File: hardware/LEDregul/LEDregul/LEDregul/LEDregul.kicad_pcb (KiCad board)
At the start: 2 copper layers, 62.7 x 57.1 mm, 45 parts, among them J1 Conn_02x04_Odd_Even, J2 Conn_01x04_Male, J4 Conn_01x20_Female, U1 FAN5341, U2 FAN5341, U3 FAN5341, U4 FAN5341, X1 SiT1534

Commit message: nRF52 start
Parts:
- moved R1 115.3 mm to (142.2, 95.2)
- moved R2 115.3 mm to (139.2, 95.2)
- moved R3 115.3 mm to (145.1, 95.2)
- moved R4 115.3 mm to (148.0, 95.2)
- moved U3 80.0 mm to (175.1, 68.6)
- moved C2 80.0 mm to (179.1, 61.8)
- moved C5 80.0 mm to (170.9, 72.0)
- moved C7 80.0 mm to (179.1, 65.1)
- moved D17 80.0 mm to (170.9, 68.7)
- moved D10 80.0 mm to (173.5, 61.9)
- moved D18 80.0 mm to (173.5, 65.3)
- moved C6 74.6 mm to (165.2, 78.8)
- moved D11 74.6 mm to (167.9, 65.3)
- moved D14 74.6 mm to (165.3, 75.5)
- moved D16 74.6 mm to (165.3, 72.1)
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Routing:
- net GND: track 198.2 -> 0.00 mm, vias 55 -> 0
- net +3V3: track 177.7 -> 0.00 mm, vias 3 -> 0
- net Net-(C1-Pad1): track 87.5 -> 0.00 mm
- net C1: track 64.9 -> 0.00 mm, vias 1 -> 0
- net Net-(D5-Pad1): track 64.4 -> 0.00 mm, vias 2 -> 0
- net Net-(C3-Pad1): track 63.3 -> 0.00 mm
- net C3: track 62.9 -> 0.00 mm, vias 1 -> 0
- net Net-(J4-Pad17): track 62.2 -> 0.00 mm
- net Net-(D15-Pad1): track 62.1 -> 0.00 mm, vias 2 -> 0
- net Net-(L2-Pad2): track 57.1 -> 0.00 mm, vias 2 -> 0
- net Net-(C7-Pad1): track 53.9 -> 0.00 mm
- net Net-(D20-Pad1): track 53.5 -> 0.00 mm
- net C2: track 51.6 -> 0.00 mm, vias 1 -> 0
- net Net-(D10-Pad1): track 46.6 -> 0.00 mm, vias 2 -> 0
- net Net-(BT1-Pad1): track 42.9 -> 0.00 mm
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- removed copper zone on B.Cu, net GND
- removed copper zone on F.Cu, net GND
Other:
- board size 62.7 x 57.1 mm -> 97.8 x 67.3 mm

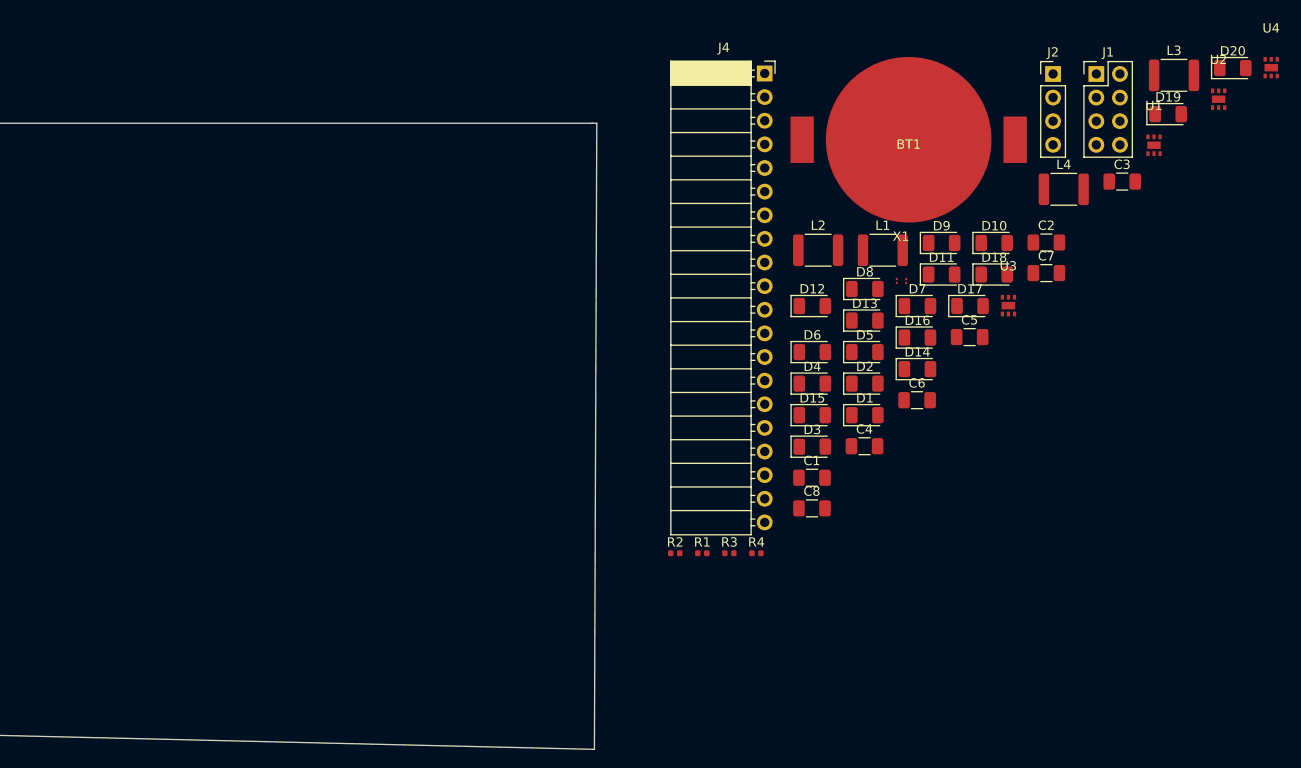
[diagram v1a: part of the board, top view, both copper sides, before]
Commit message: THS5641, ADC08100, ADC08060 boards
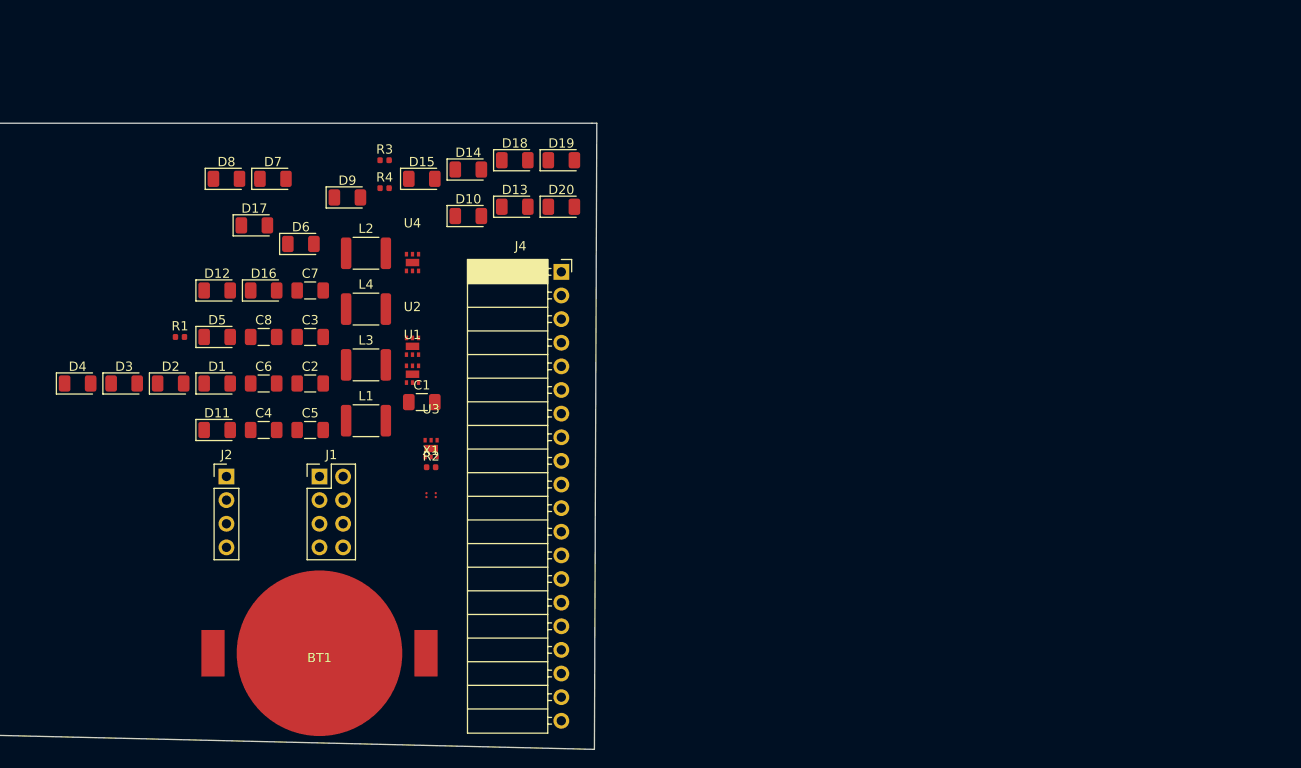
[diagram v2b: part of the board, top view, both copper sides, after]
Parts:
- moved J2 98.8 mm to (91.0, 87.0)
- moved U4 94.7 mm to (111.0, 64.0)
- moved J1 94.1 mm to (101.0, 87.0)
- moved L3 92.3 mm to (106.0, 75.0)
- moved U2 90.6 mm to (111.0, 73.0)
- moved C3 88.9 mm to (100.0, 72.0)
- moved BT1 84.0 mm to (101.0, 106.0)
- moved U1 83.4 mm to (111.0, 76.0)
- moved C2 80.6 mm to (100.0, 77.0)
- moved D11 79.7 mm to (90.0, 82.0)
- moved C7 79.2 mm to (100.0, 67.0)
- moved D4 79.0 mm to (75.0, 77.0)
- moved D17 77.4 mm to (94.0, 60.0)
- moved L4 76.1 mm to (106.0, 69.0)
- moved D2 74.6 mm to (85.0, 77.0)
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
